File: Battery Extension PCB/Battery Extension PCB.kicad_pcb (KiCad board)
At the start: 2 copper layers, 76.5 x 16.7 mm, 30 parts, among them P1 Solder_Pad, P2 Solder_Pad, U1 M1250RS-02P, U2 S8050, U3 FS8205A, U4 TPS61032PWPR, U5 TP4056, U6 DW01A, U7 FXL0530-6R8-M

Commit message: updated pcb files
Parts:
- H1, H2, H3, H4, H5, H6, H7: footprint footprint:Castellated hole large -> footprint:Castellated hole
- U4: footprint footprint:HTSSOP-16_L5.0-W4.4-P0.65-LS6.4-BL-EP -> Package_SO:HTSSOP-16-1EP_4.4x5mm_P0.65mm_EP3.4x5mm_Mask2.46x2.31mm
- turned U4 to 0 degrees
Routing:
- net Net-(R4-Pad2): track 23.3 -> 25.6 mm
- net (no net): vias 0 -> 2

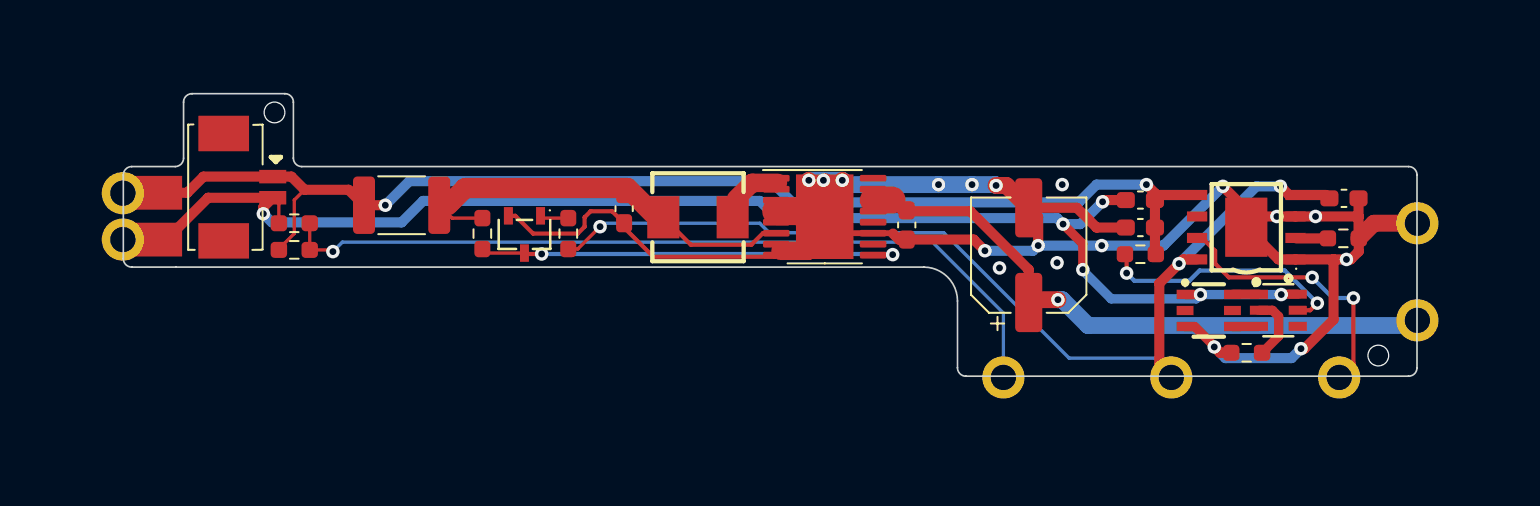
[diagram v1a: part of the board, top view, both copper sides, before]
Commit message: replaced castallated holes with solder pads
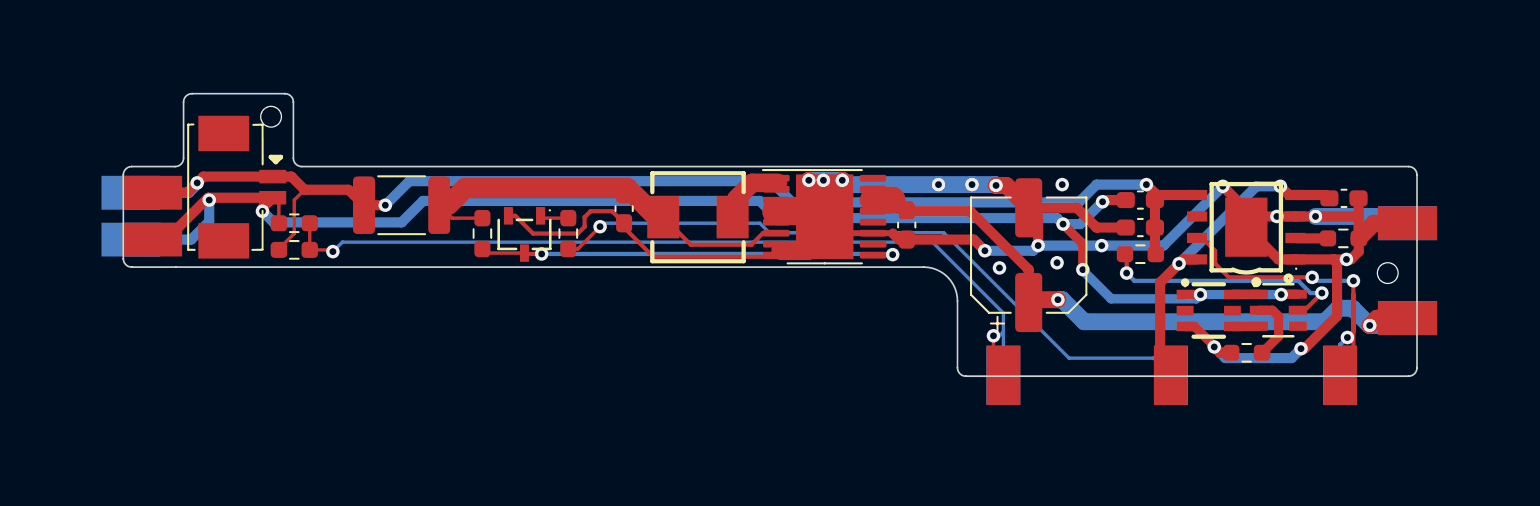
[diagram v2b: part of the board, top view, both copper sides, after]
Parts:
- removed H1, H2, H3, H4, H5, H6, H7: Castellated_hole, footprint:Castellated hole
- added P10: Solder_Pad, footprint:Solder pad, B.Cu at (118.3, 80.7)
- added P11: Solder_Pad, footprint:Solder pad, F.Cu at (138.2, 80.8)
- added P12: Solder_Pad, footprint:Solder pad, F.Cu at (142.2, 77.3)
- added P13: Solder_Pad, footprint:Solder pad, F.Cu at (142.2, 71.7)
- added P14: Solder_Pad, footprint:Solder pad, B.Cu at (128.2, 80.7)
- added P3: Solder_Pad, footprint:Solder pad, F.Cu at (118.3, 80.8)
- added P4: Solder_Pad, footprint:Solder pad, B.Cu at (138.2, 80.7)
- added P5: Solder_Pad, footprint:Solder pad, B.Cu at (142.3, 77.3)
- added P6: Solder_Pad, footprint:Solder pad, B.Cu at (142.2, 71.8)
- added P7: Solder_Pad, footprint:Solder pad, F.Cu at (128.2, 80.8)
- added P8: Solder_Pad, footprint:Solder pad, B.Cu at (66.8, 69.8)
- added P9: Solder_Pad, footprint:Solder pad, B.Cu at (66.8, 72.6)
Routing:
- net GND: track 122.4 -> 130.1 mm
- net IO27/BATT CHARGING: track 16.1 -> 21.7 mm, vias 2 -> 3
- net -BATT: track 83.0 -> 88.2 mm, vias 6 -> 7
- net IO26/BATT VOLT: track 48.2 -> 51.5 mm, vias 1 -> 2
- net +5V: track 36.7 -> 39.9 mm, vias 1 -> 2
- net +BATT: track 74.0 -> 77.0 mm, vias 2 -> 3

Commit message: updated pcb
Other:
- board text added: "PCB files: https://bit.ly/ xxxx"
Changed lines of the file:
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@@
       (drillshape 0)
       (scaleselection 1)
-      (outputdirectory "jlcpcb/gerber/")
+      (outputdirectory "jlcpcb/gerber tinted vias/")
     )
   )
@@
   (gr_line locked (start 142.299615 80.773967) (end 116.125445 80.773967) (layer "Edge.Cuts") (width 0.1))
   (gr_line locked (start 66.29454 73.822228) (end 66.29454 68.8768) (layer "Edge.Cuts") (width 0.1))
+  (gr_text "PCB files:\nhttps://bit.ly/\nxxxx" (at 139.1412 55.0164) (layer "B.SilkS")
+    (effects (font (size 0.8 0.8) (thickness 0.15)) (justify left mirror))
+  )
   (gr_text "5V" (at 142.1892 79.3496) (layer "B.SilkS")
     (effects (font (size 1 1) (thickness 0.15)) (justify left mirror))
@@
     )
   )
+  (group "" (id 24c1ed49-d0fc-4375-9671-341cd4e5cea3)
+    (members
+      03cb480e-8c24-48d7-8b7f-5a0b3bf98f73
+    )
+  )

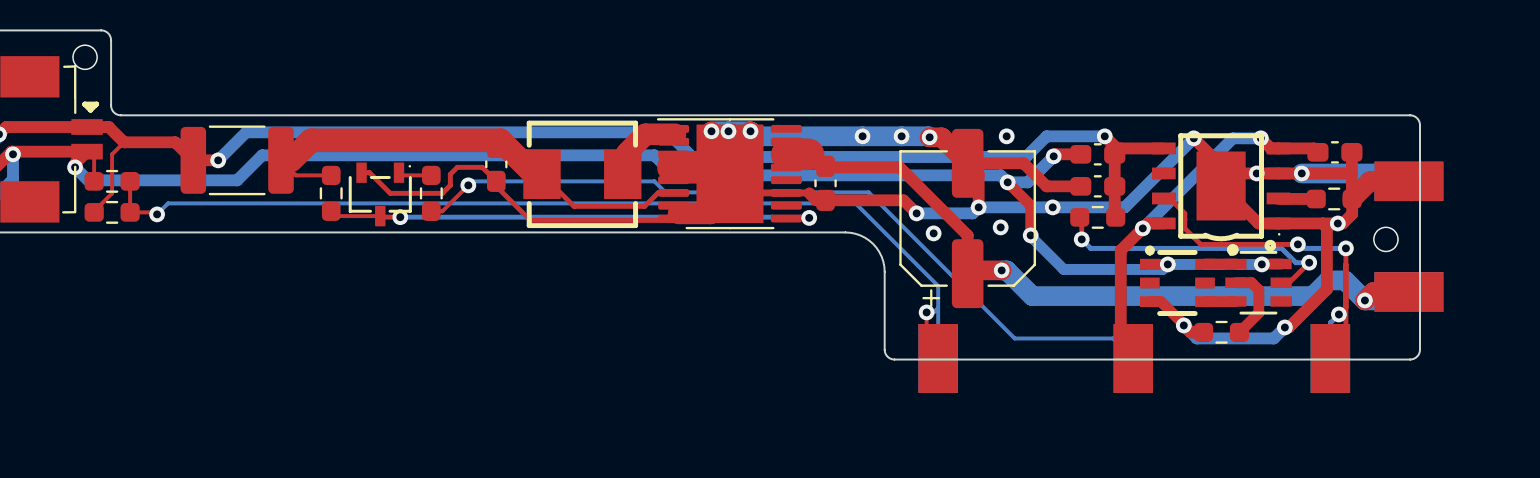
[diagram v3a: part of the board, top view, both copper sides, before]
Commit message: fixed battery extension
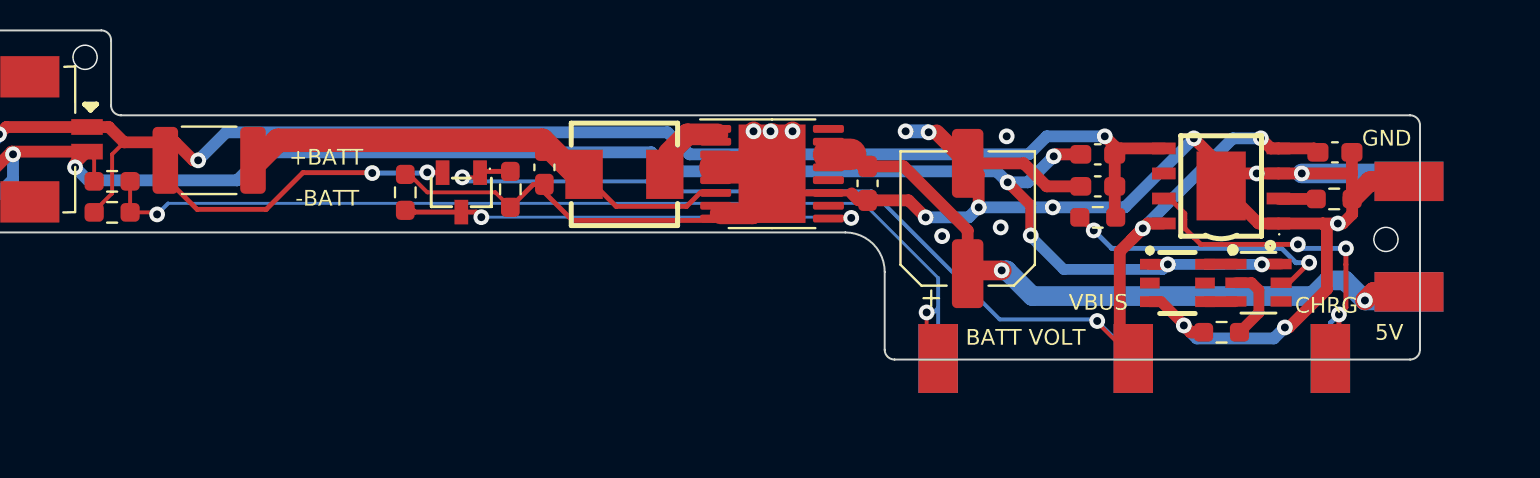
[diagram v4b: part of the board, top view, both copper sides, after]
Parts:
- removed R3, R4: 100K, Resistor_SMD:R_0603_1608Metric_Pad0.98x0.95mm_HandSolder
- removed U2: S8050, footprint:SOT-23-3_L3.0-W1.7-P0.95-LS2.9-BR
- added R6: 100K, Resistor_SMD:R_0603_1608Metric_Pad0.98x0.95mm_HandSolder, F.Cu at (96.6, 72.1)
- added R9: 100K, Resistor_SMD:R_0603_1608Metric_Pad0.98x0.95mm_HandSolder, F.Cu at (91.3, 72.3)
- added U8: AP40P05, footprint:SOT-23-3_L2.9-W1.3-P1.90-LS2.4-BR, F.Cu at (94.1, 72.3)
- moved C2 2.44 mm to (98.3, 71.0)
- moved C3 2.13 mm to (114.8, 71.8)
- moved U4 2.13 mm to (109.9, 71.3)
- moved U7 2.13 mm to (102.4, 71.4)
- moved F1 1.42 mm to (81.3, 70.7)
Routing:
- net +BATT: track 77.0 -> 93.3 mm, vias 3 -> 5
- net GND: track 130.1 -> 118.2 mm, vias 18 -> 17
- net VBUS: track 59.3 -> 64.5 mm, vias 3 -> 4
- net IO27/BATT CHARGING: track 21.7 -> 18.9 mm
- net +5V: track 39.9 -> 37.9 mm
- net Net-(R3-Pad2): track 1.70 -> 0.00 mm
- net Net-(R9-Pad1): track 25.6 -> 24.1 mm
- net Net-(R8-Pad1): track 15.0 -> 14.4 mm
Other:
- board text added: "BATT CHRG"
- board text added: "BATT VOLT"
- board text added: "CHRG"
- board text added: "GlowSign Battery Extension v1.1"
- board text added: "PCB files: https://bit.ly/3EajZGV"
- board text removed: "GlowSign Battery Extension v1.0"
- board text removed: "IO26/ BATT VOLT"
- board text removed: "IO27/ BATT CHARG"
- board text removed: "PCB files: https://bit.ly/ xxxx"

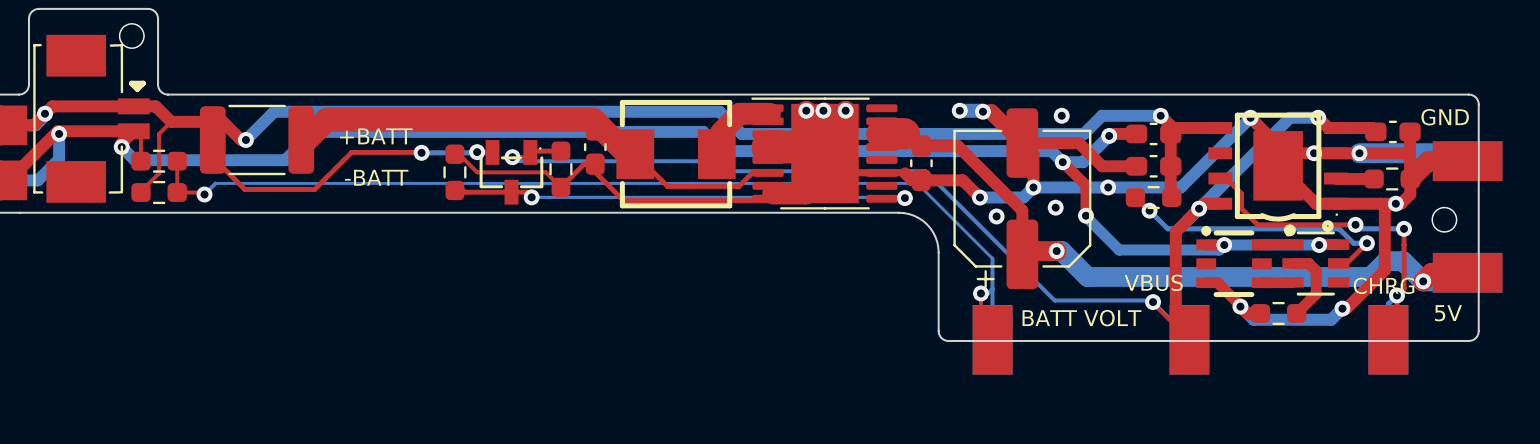
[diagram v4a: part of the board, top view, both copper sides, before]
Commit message: replaced 0603 with 0402 (battery extension)
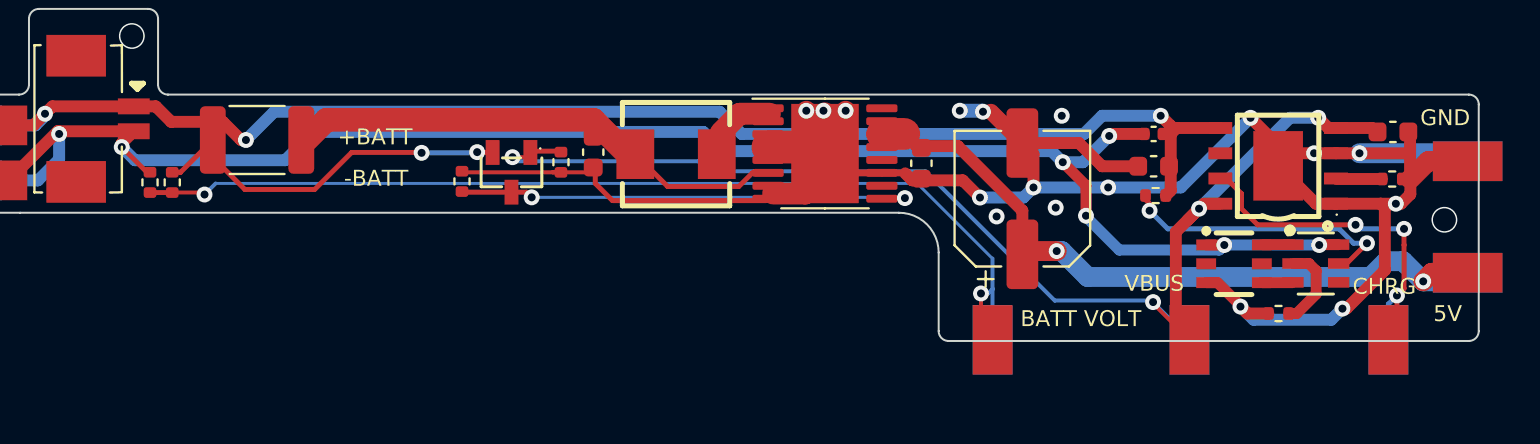
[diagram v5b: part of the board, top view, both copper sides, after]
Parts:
- C1, C2, C3, C4: footprint Capacitor_SMD:C_0603_1608Metric_Pad1.08x0.95mm_HandSolder -> Capacitor_SMD:C_0603_1608Metric
- C5: footprint Capacitor_SMD:C_0603_1608Metric_Pad1.08x0.95mm_HandSolder -> Capacitor_SMD:C_0402_1005Metric
- R1, R2, R5, R6, R8, R9: footprint Resistor_SMD:R_0603_1608Metric_Pad0.98x0.95mm_HandSolder -> Resistor_SMD:R_0402_1005Metric
- R7: value 5.1K -> 2K; footprint Resistor_SMD:R_0603_1608Metric_Pad0.98x0.95mm_HandSolder -> Resistor_SMD:R_0402_1005Metric
- moved R2 1.16 mm to (75.9, 72.8), turned to -90 degrees
- moved R1 0.83 mm to (77.1, 72.8), turned to 90 degrees
- moved R9 0.58 mm to (91.6, 72.7)
- moved R6 0.36 mm to (96.6, 71.8)
- moved C2 0.27 mm to (98.2, 71.3)
- moved R8 0.14 mm to (126.5, 73.5)
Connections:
- net IO26/BATT VOLT renamed BATT VOLT
- net IO27/BATT CHARGING renamed BATT CHARGING
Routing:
- net +BATT: track 93.3 -> 91.8 mm
- net GND: track 118.2 -> 117.4 mm
- net -BATT: track 88.3 -> 89.0 mm

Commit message: updated pcb designs
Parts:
- added R3: 100K, Resistor_SMD:R_0402_1005Metric, F.Cu at (79.3, 73.5)
- added U2: AP40P05, footprint:SOT-23-3_L2.9-W1.3-P1.90-LS2.4-BR, F.Cu at (76.4, 72.4)
- R1: value 100K -> 33K
- moved R1 7.34 mm to (84.4, 73.5), turned to 0 degrees
- moved R2 5.43 mm to (81.3, 73.5), turned to 0 degrees
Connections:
- P1 pad 1: +BATT -> Net-(P1-Pad1)
- P8 pad 1: +BATT -> Net-(P1-Pad1)
- U1 pad 1: +BATT -> Net-(P1-Pad1)
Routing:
- net Net-(P1-Pad1): track 0.00 -> 17.2 mm, vias 0 -> 1
- net +BATT: track 91.8 -> 75.1 mm, vias 5 -> 4
- net BATT VOLT: track 51.7 -> 46.8 mm
- net -BATT: track 89.0 -> 92.3 mm, vias 7 -> 8
- net Net-(R3-Pad2): track 0.00 -> 1.41 mm
